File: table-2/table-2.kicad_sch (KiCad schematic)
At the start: 33 parts, among them J1 1.8" OLED DISPLAY, J10 LED Strip Connector, J11 PSU screw terminal, J2 USB_A_Stacked, J3 MPU6050, J4 Ultrasonic Sensor, J7 Dual H-Bridge Control, J8 USB_C_Receptacle_PowerOnly_6P, J9 Dual H-Brdige Power, SW1 SW_Push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

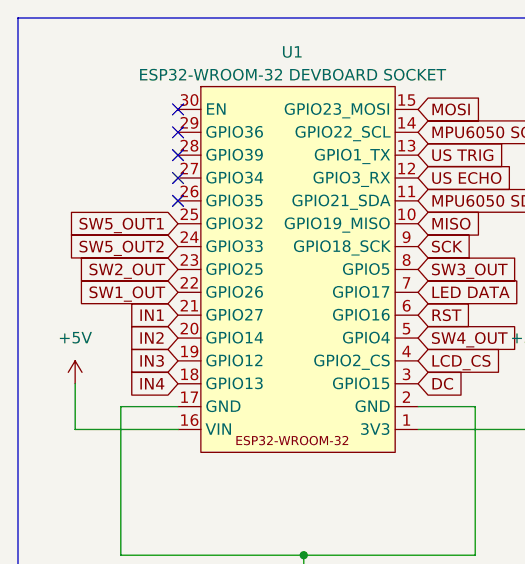
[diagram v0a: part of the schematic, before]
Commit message: forgot about the backside of the pcb. this is one much smaller and denser
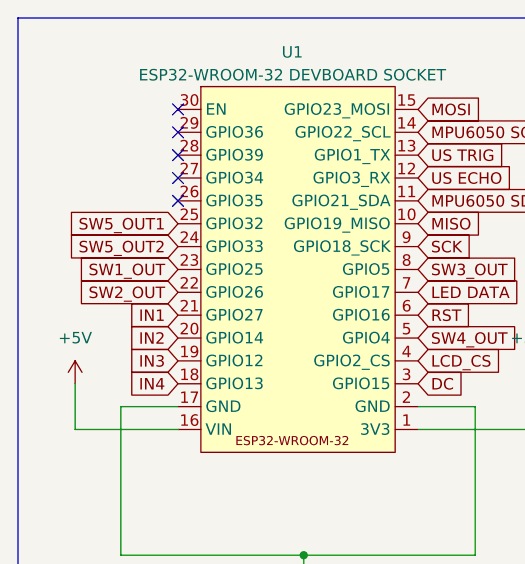
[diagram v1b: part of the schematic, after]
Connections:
- net SW1_OUT: now also U1.23 (GPIO25); no longer U1.22 (GPIO26)
- net SW2_OUT: now also U1.22 (GPIO26); no longer U1.23 (GPIO25)
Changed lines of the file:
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@@
+		)
+	)
+	(global_label "SW2_OUT"
+		(shape input)
+		(at 31.75 44.45 180)
+		(fields_autoplaced yes)
+		(effects
+			(font
+				(size 1.27 1.27)
+			)
+			(justify right)
+		)
+		(property "Intersheetrefs" "${INTERSHEET_REFS}"
+			(at 20.2982 44.45 0)
+			(effects
+				(font
+					(size 1.27 1.27)
+				)
+				(justify right)
+				(hide yes)
+			)
 		)
 	)
@@
 		)
 	)
-	(global_label "SW2_OUT"
+	(global_label "SW1_OUT"
 		(shape input)
 		(at 31.75 41.91 180)
@@
 				(hide yes)
 			)
-		)
-	)
-	(global_label "SW1_OUT"
-		(shape input)
-		(at 31.75 44.45 180)
-		(fields_autoplaced yes)
-		(effects
-			(font
-				(size 1.27 1.27)
-			)
-			(justify right)
-		)
-		(property "Intersheetrefs" "${INTERSHEET_REFS}"
-			(at 20.2982 44.45 0)
-			(effects
-				(font
-					(size 1.27 1.27)
-				)
-				(justify right)
-				(hide yes)
-			)
